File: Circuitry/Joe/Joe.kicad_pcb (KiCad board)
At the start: 2 copper layers, 51.1 x 107.3 mm, 33 parts, among them J1 Conn_02x03_Counter_Clockwise, J2 Conn_01x20, J3 USB_B_Micro, J4 Micro_SD_Card, U5 DS3231MZ, U6 M24C32-XDW5TP, U7 DF12-20DS, U8 AP2127N-3.3, U9 ATmega32U4-MU

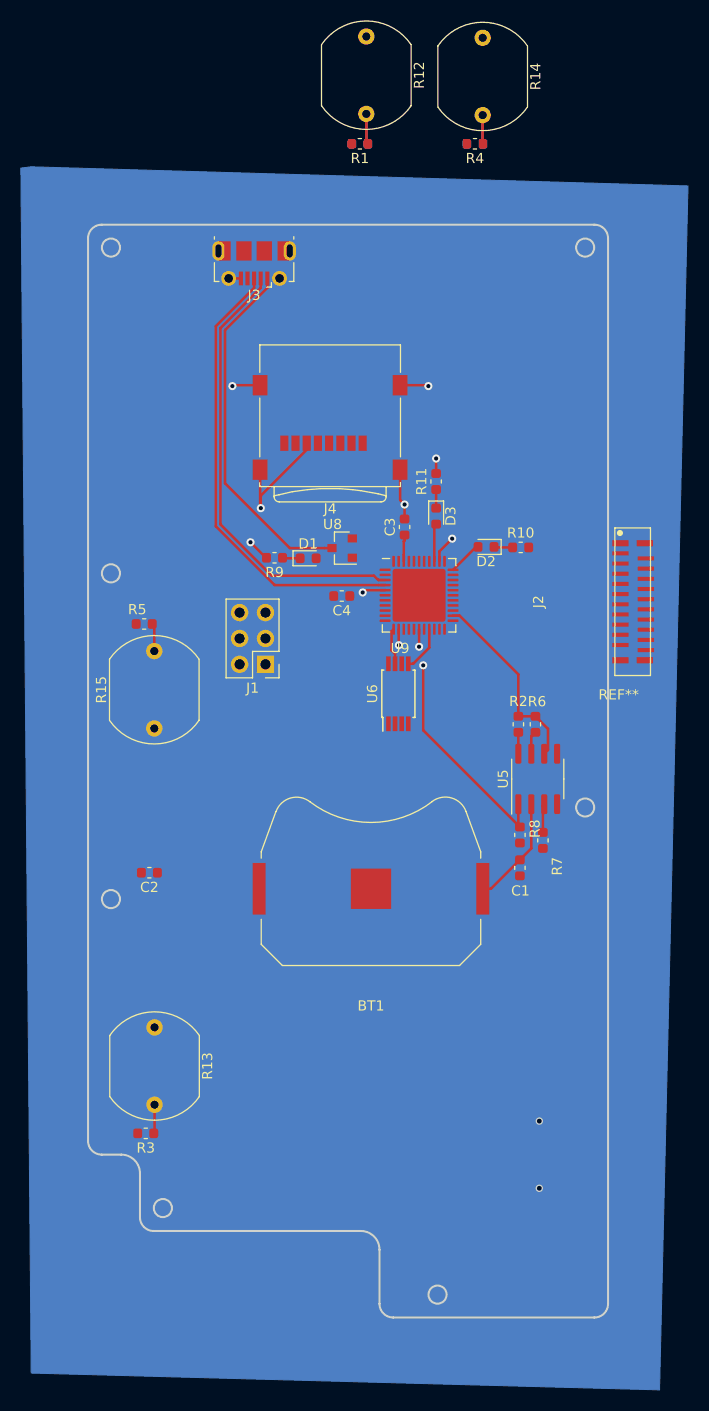
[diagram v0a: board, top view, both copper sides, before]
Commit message: completed joe layout for review; addresses for dcf
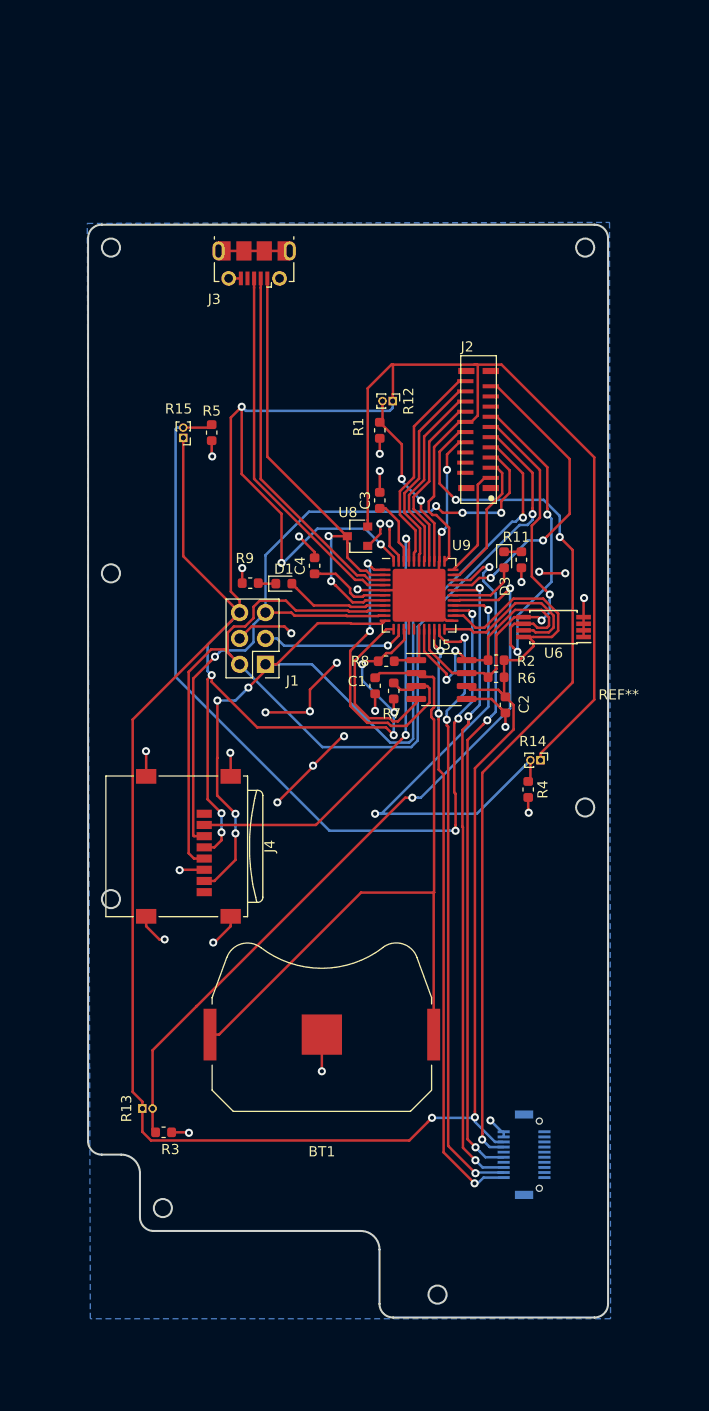
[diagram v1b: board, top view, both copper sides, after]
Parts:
- removed D2: LED, LED_SMD:LED_0603_1608Metric
- removed R10: 440R, Resistor_SMD:R_0603_1608Metric
- R12, R14, R15: footprint OptoDevice:R_LDR_10x8.5mm_P7.6mm_Vertical -> Connector_PinHeader_1.00mm:PinHeader_1x02_P1.00mm_Vertical
- R13: footprint OptoDevice:R_LDR_10x8.5mm_P7.6mm_Vertical -> Connector_PinHeader_1.00mm:PinHeader_1x02_P1.00mm_Vertical; moved to B.Cu
- moved R14 71.2 mm to (-7.67, 6.93)
- moved R4 63.6 mm to (-8.89, 9.80), turned to 270 degrees
- moved J4 43.4 mm to (-42.3, 15.4), turned to 270 degrees
- moved C2 38.7 mm to (-11.1, 1.50), turned to 270 degrees
- moved R12 35.9 mm to (-22.2, -28.3)
- moved R15 28.7 mm to (-42.8, -24.7), turned to 180 degrees
- moved R1 28.2 mm to (-23.5, -25.5), turned to 270 degrees
- moved C1 22.8 mm to (-23.9, -0.38)
- moved J2 22.7 mm to (-13.8, -25.6), turned to 270 degrees
- moved R8 21.5 mm to (-22.8, -2.79), turned to 0 degrees
- moved R7 20.7 mm to (-22.1, 0.13)
- moved R5 19.9 mm to (-40.0, -25.2), turned to 270 degrees
- moved U6 16.6 mm to (-6.40, -6.15), turned to 180 degrees
- moved BT1 15.1 mm to (-29.2, 33.9)
- moved U5 13.6 mm to (-17.4, -0.99), turned to 0 degrees
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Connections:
- J2 pad 8: /BP1 -> Net-(J2-Pad8)
- J2 pad 9: /BP2 -> Net-(J2-Pad9)
- U9 pad 12: /WC -> /TMR_RST
- U9 pad 22: /TMR_RST -> /WC
- U9 pad 28: /PHO1 -> /PLED3
- U9 pad 29: /BP1 -> /BUSY
- U9 pad 30: /BP2 -> /SER
- U9 pad 32: /~CS_SD -> /CS_IMG
- U9 pad 33: /PLED2 -> /TEMP
- U9 pad 36: /PLED3 -> /PHO1
- U9 pad 37: /SER -> /IN2
- U9 pad 38: /BUSY -> /IN1
- U9 pad 41: Net-(U9-Pad41) -> /~CS_SD
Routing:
- net +3V3: track 18.9 -> 417.8 mm, vias 0 -> 11
- net /SCK: track 0.00 -> 104.5 mm, vias 0 -> 1
- net /MISO: track 0.00 -> 93.4 mm, vias 0 -> 5
- net +5V: track 0.00 -> 87.5 mm, vias 0 -> 3
- net GND: track 32.6 -> 119.2 mm, vias 8 -> 32
- net /PHO4: track 2.75 -> 85.9 mm, vias 0 -> 3
- net /MOSI: track 0.00 -> 77.2 mm, vias 0 -> 4
- net /PHO2: track 2.85 -> 75.4 mm, vias 0 -> 2
- net /STBY: track 0.00 -> 66.5 mm, vias 0 -> 3
- net /BUSY: track 0.00 -> 63.2 mm, vias 0 -> 3
- net /TX: track 0.00 -> 60.9 mm, vias 0 -> 3
- net /RX: track 0.00 -> 59.3 mm, vias 0 -> 3
- net Net-(BT1-Pad1): track 10.8 -> 69.9 mm
- net /SCL: track 2.11 -> 57.3 mm, vias 0 -> 4
- net /~CS_SD: track 0.00 -> 46.3 mm, vias 0 -> 2
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- added copper zone on B.Cu, net GND

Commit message: complete joe layoutgit add .git add .git add . woooohooooooo!
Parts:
- added ?: , , F.Cu at (-5.31, 44.5)
- R12: value R_PHOTO -> P1; footprint Connector_PinHeader_1.00mm:PinHeader_1x02_P1.00mm_Vertical -> Custom:PinHeader_1x02_P1.00mm_Vertical
- R13, R14: value R_PHOTO -> P3; footprint Connector_PinHeader_1.00mm:PinHeader_1x02_P1.00mm_Vertical -> Custom:PinHeader_1x02_P1.00mm_Vertical
- R15: value R_PHOTO -> P4; footprint Connector_PinHeader_1.00mm:PinHeader_1x02_P1.00mm_Vertical -> Custom:PinHeader_1x02_P1.00mm_Vertical
- U7: value DF12-20DS -> NSL BUS
- moved R12 65.6 mm to (-47.9, 32.1), turned to 90 degrees
- moved R1 61.5 mm to (-42.5, 33.0)
- moved R5 55.4 mm to (-44.7, 30.0)
- moved R15 54.5 mm to (-47.8, 29.6), turned to 90 degrees
- moved R14 37.1 mm to (-43.5, -2.84), turned to 180 degrees
- moved R4 34.3 mm to (-40.2, -4.11), turned to 0 degrees
- moved R9 27.3 mm to (-9.42, -16.0), turned to 90 degrees
- moved D1 23.5 mm to (-9.50, -12.7), turned to 270 degrees
- moved R3 19.1 mm to (-47.2, 24.6), turned to 180 degrees
- moved J2 18.2 mm to (-31.4, -30.0), turned to 90 degrees
- moved R13 14.1 mm to (-47.8, 27.1)
- moved BT1 7.80 mm to (-31.6, 41.3)
- moved J1 6.13 mm to (-28.8, -0.81)
- moved J4 4.84 mm to (-42.7, 10.6)
- moved R11 3.67 mm to (-11.2, -16.0), turned to 90 degrees
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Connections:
- J1 pad 2: /SCK -> +3V3
- J1 pad 3: /RST -> /SCK
- J1 pad 4: GND -> /MOSI
- J1 pad 5: /MOSI -> /RST
- J1 pad 6: +3V3 -> GND
- U7 pad 11: /RX -> /TX
- U7 pad 12: /TX -> /RX
- U9 pad 20: /RX -> /TX
- U9 pad 21: /TX -> /RX
- U9 pad 26: /PHO3 -> /PHO1
- U9 pad 27: /PHO2 -> /PLED1
- U9 pad 36: /PHO1 -> /PHO2
- U9 pad 8: /PLED1 -> /PHO3
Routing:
- net +3V3: track 417.8 -> 108.2 mm, vias 11 -> 14
- net /SDA: track 41.5 -> 87.3 mm
- net /PHO1: track 18.1 -> 61.9 mm
- net /SCK: track 104.5 -> 63.2 mm, vias 1 -> 3
- net /PHO4: track 85.9 -> 55.3 mm, vias 3 -> 2
- net GND: track 119.2 -> 93.2 mm, vias 32 -> 24
- net /PHO3: track 48.2 -> 22.2 mm, vias 2 -> 0
- net /CS_IMG: track 13.7 -> 39.6 mm
- net /SCL: track 57.3 -> 82.0 mm
- net /MISO: track 93.4 -> 72.0 mm, vias 5 -> 2
- net /TEMP: track 10.9 -> 31.9 mm
- net /PHO2: track 75.4 -> 62.3 mm
- net /MOSI: track 77.2 -> 64.9 mm, vias 4 -> 2
- net +5V: track 87.5 -> 96.5 mm
- net Net-(BT1-Pad1): track 69.9 -> 76.9 mm
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- added copper zone on F.Cu, net +3V3
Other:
- board text added: "Dhara Patel V1"
- board text added: "NSL BUS"
- board text added: "PLED1"
- board text added: "PLED2"
